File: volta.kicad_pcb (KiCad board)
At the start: 2 copper layers, 105 x 100 mm, 12 parts, among them J1 , J2 , T1 5:1 - 5A

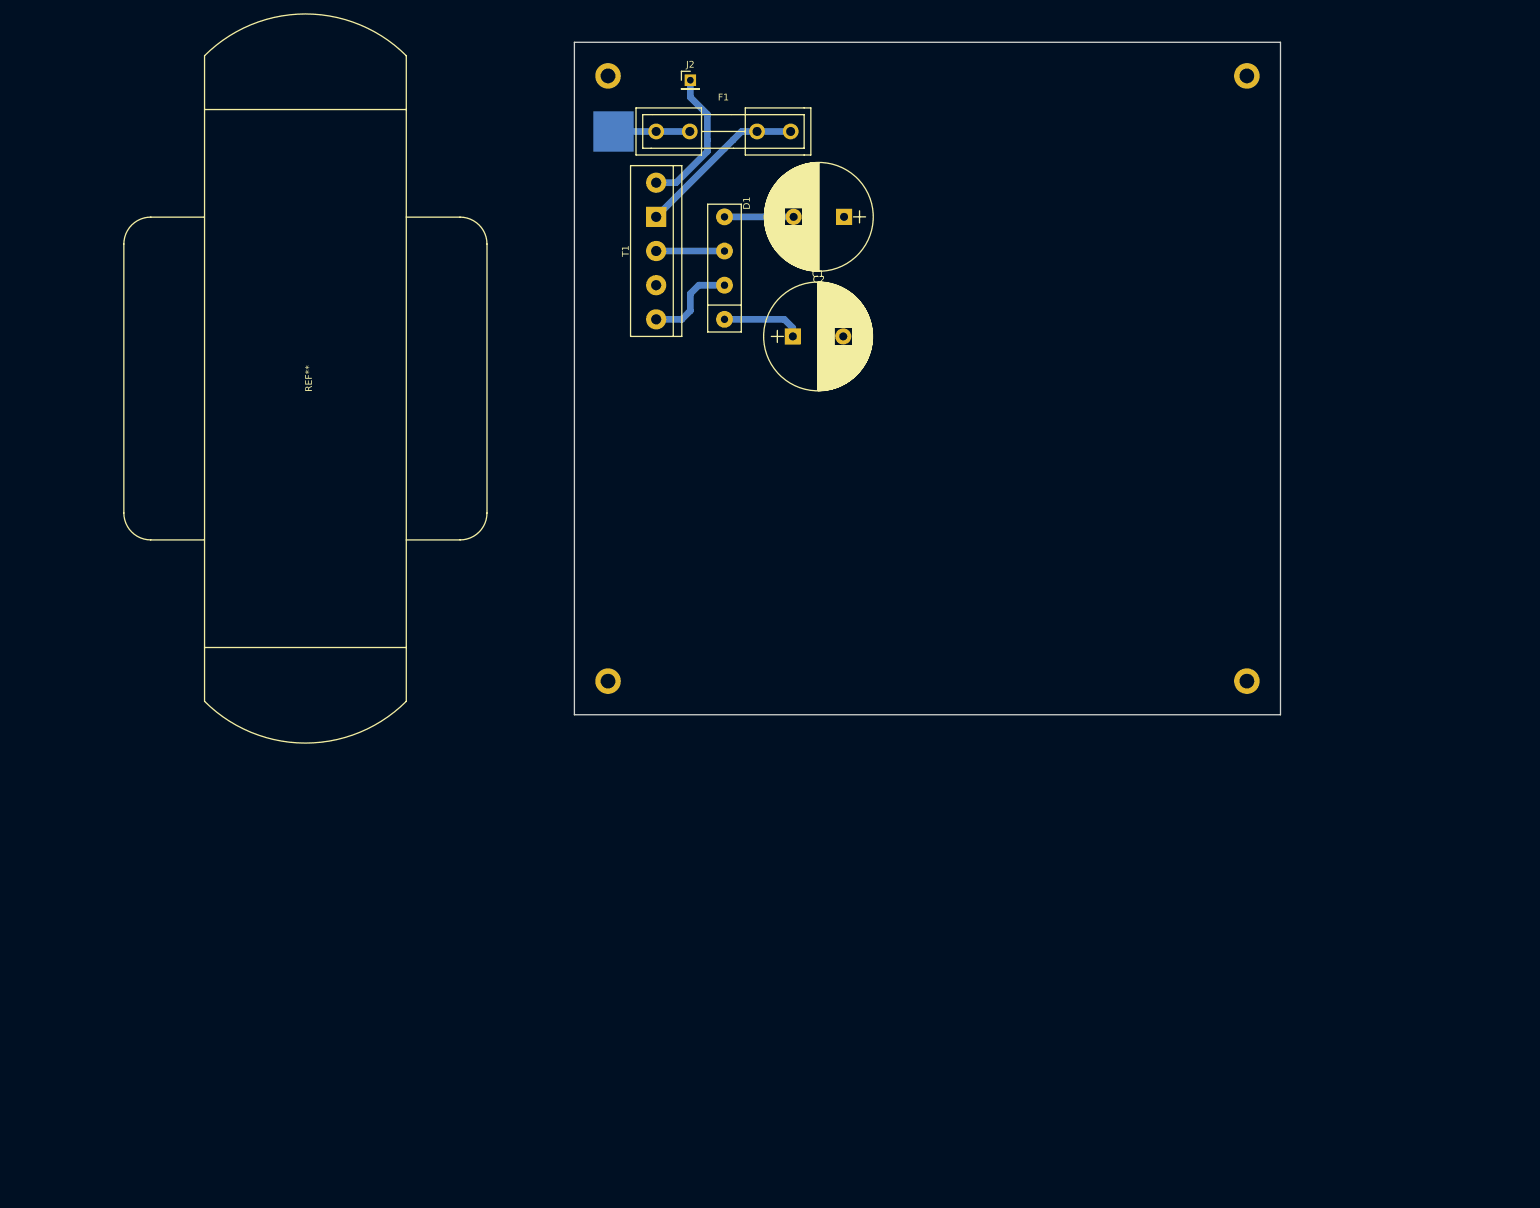
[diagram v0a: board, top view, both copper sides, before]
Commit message: Trabajo
 Cambios para hacer commit:
	modificado:    volta-cache.lib
	modificado:    volta.kicad_pcb
	modificado:    volta.pro
	modificado:    volta.sch
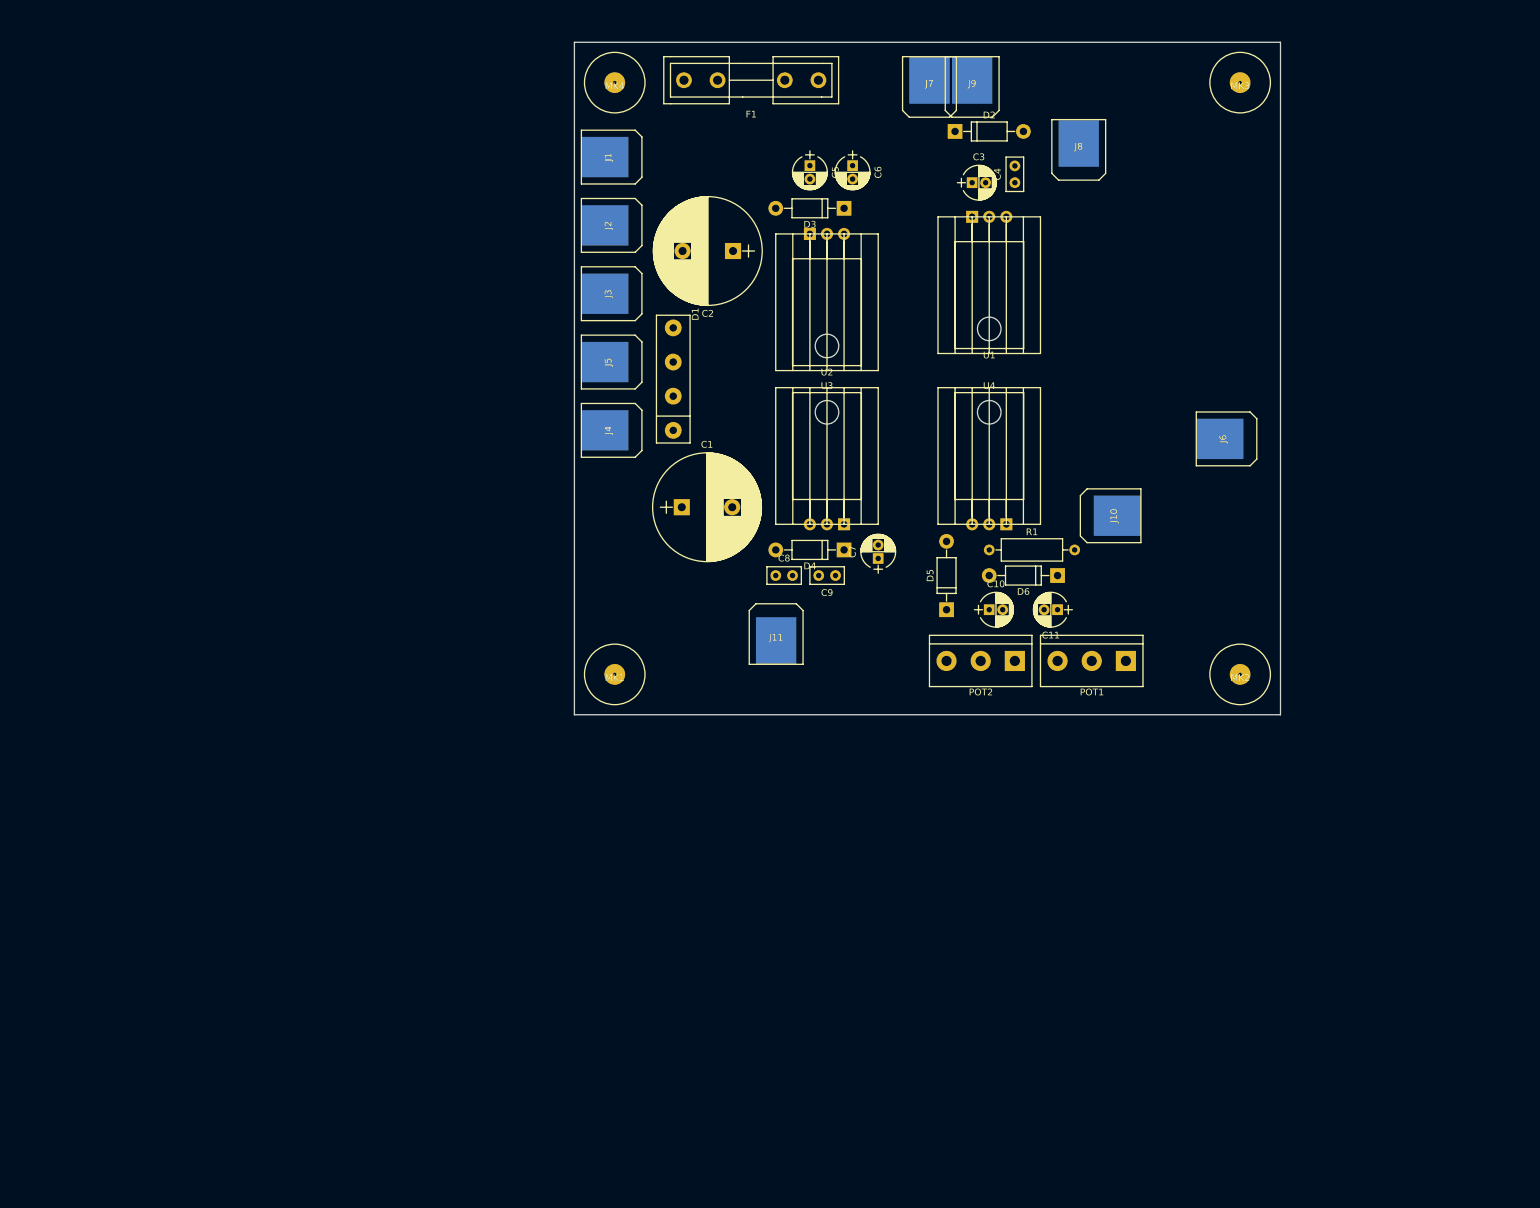
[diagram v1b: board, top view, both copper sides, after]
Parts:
- removed REF**: EXI_Transformador_1_Derivacion_80x30mm, EXI_Transformadores:EXI_Transformador_1_Derivacion_80x30mm
- removed REF** (x4): MountingHole_2.2mm_M2_DIN965_Pad, Mounting_Holes:MountingHole_2.2mm_M2_DIN965_Pad
- removed T1: 5:1 - 5A, TerminalBlock:TerminalBlock_bornier-5_P5.08mm
- added C10: 1uF, Capacitors_THT:CP_Radial_D5.0mm_P2.00mm, F.Cu at (186.7, 119.4)
- added C11: 10uF, Capacitors_THT:CP_Radial_D5.0mm_P2.00mm, F.Cu at (196.8, 119.4)
- added C3: 0.33uF, Capacitors_THT:CP_Radial_D5.0mm_P2.00mm, F.Cu at (184.2, 55.9)
- added C4: 0.1uF, Capacitors_THT:C_Disc_D5.0mm_W2.5mm_P2.50mm, F.Cu at (190.5, 55.9)
- added C5: 22uF / 25V, Capacitors_THT:CP_Radial_D5.0mm_P2.00mm, F.Cu at (160.0, 53.3)
- added C6: 1uF, Capacitors_THT:CP_Radial_D5.0mm_P2.00mm, F.Cu at (166.4, 53.3)
- added C7: 0.33uF, Capacitors_THT:CP_Radial_D5.0mm_P2.00mm, F.Cu at (170.2, 111.8)
- added C8: 0.1uF, Capacitors_THT:C_Disc_D5.0mm_W2.5mm_P2.50mm, F.Cu at (154.9, 114.3)
- added C9: 0.1uF, Capacitors_THT:C_Disc_D5.0mm_W2.5mm_P2.50mm, F.Cu at (163.8, 114.3)
- added D2: 1N4007, Diodes_THT:D_DO-41_SOD81_P10.16mm_Horizontal, F.Cu at (181.6, 48.3)
- added D3: 1N4007, Diodes_THT:D_DO-41_SOD81_P10.16mm_Horizontal, F.Cu at (165.1, 59.7)
- added D4: 1N4007, Diodes_THT:D_DO-41_SOD81_P10.16mm_Horizontal, F.Cu at (165.1, 110.5)
- added D5: 1N4007, Diodes_THT:D_DO-41_SOD81_P10.16mm_Horizontal, F.Cu at (180.3, 119.4)
- added D6: 1N4007, Diodes_THT:D_DO-41_SOD81_P10.16mm_Horizontal, F.Cu at (196.8, 114.3)
- added J10: +Vv, EXI_Conectores:EXI_Pad_6x7mm_x1, F.Cu at (205.7, 105.4)
- added J11: +5V, EXI_Conectores:EXI_Pad_6x7mm_x1, F.Cu at (155.0, 124.0)
- added J3: Deriv, EXI_Conectores:EXI_Pad_6x7mm_x1, F.Cu at (129.5, 72.4)
- added J4: Trans-V24, EXI_Conectores:EXI_Pad_6x7mm_x1, F.Cu at (129.5, 92.7)
- added J5: Trans-N24, EXI_Conectores:EXI_Pad_6x7mm_x1, F.Cu at (129.5, 82.5)
- added J6: GND, EXI_Conectores:EXI_Pad_6x7mm_x1, F.Cu at (221.0, 94.0)
- added J7: V-, EXI_Conectores:EXI_Pad_6x7mm_x1, F.Cu at (177.8, 40.6)
- added J8: +12, EXI_Conectores:EXI_Pad_6x7mm_x1, F.Cu at (200.0, 50.0)
- added J9: -12, EXI_Conectores:EXI_Pad_6x7mm_x1, F.Cu at (184.2, 40.6)
- added MK1: Mounting_Hole, EXI_Montaje:Tuerca_9mm, F.Cu at (131.0, 129.0)
- added MK2: Mounting_Hole, EXI_Montaje:Tuerca_9mm, F.Cu at (224.0, 129.0)
- added MK3: Mounting_Hole, EXI_Montaje:Tuerca_9mm, F.Cu at (224.0, 41.0)
- added MK4: Mounting_Hole, EXI_Montaje:Tuerca_9mm, F.Cu at (131.0, 41.0)
- added POT1: 5k, TerminalBlock:TerminalBlock_bornier-3_P5.08mm, F.Cu at (207.0, 127.0)
- added POT2: 1k, TerminalBlock:TerminalBlock_bornier-3_P5.08mm, F.Cu at (190.5, 127.0)
- added R1: 120, Resistors_THT:R_Axial_DIN0309_L9.0mm_D3.2mm_P12.70mm_Horizontal, F.Cu at (186.7, 110.5)
- added U1: L7812, EXI_Transistores:TO-220-3_Horizontal_Heatsink_10x15x21mm, F.Cu at (186.7, 61.0)
- added U2: L7912, EXI_Transistores:TO-220-3_Horizontal_Heatsink_10x15x21mm, F.Cu at (162.6, 63.5)
- added U3: L7805, EXI_Transistores:TO-220-3_Horizontal_Heatsink_10x15x21mm, F.Cu at (162.6, 106.7)
- added U4: LM338T, EXI_Transistores:TO-220-3_Horizontal_Heatsink_10x15x21mm, F.Cu at (186.7, 106.7)
- J1: value (none) -> AC-vivo; footprint EXI_Conectores:EXI_Pad_6x6mm -> EXI_Conectores:EXI_Pad_6x7mm_x1; moved to F.Cu
- J2: value (none) -> Trans-Vivo; footprint Pin_Headers:Pin_Header_Straight_1x01_Pitch2.54mm -> EXI_Conectores:EXI_Pad_6x7mm_x1
- moved C1 30.3 mm to (141.0, 104.1)
- moved F1 25.3 mm to (161.3, 40.6), turned to 180 degrees
- moved J2 25.0 mm to (129.5, 62.2), turned to 90 degrees
- moved D1 18.2 mm to (139.7, 85.1)
- moved C2 17.3 mm to (148.6, 66.0)
- moved J1 4.02 mm to (129.5, 52.1)
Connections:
- net Net-(C1-Pad1) renamed /V+
- net Net-(C2-Pad2) renamed /V-
- J2 pad 1: Net-(J2-Pad1) -> Net-(F1-Pad2)
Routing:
- net Net-(F1-Pad2): track 25.3 -> 0.00 mm
- net Net-(J2-Pad1): track 21.2 -> 0.00 mm
- net Net-(D1-Pad2): track 13.8 -> 0.00 mm
- net /V+: track 12.0 -> 0.00 mm
- net Net-(F1-Pad1): track 11.3 -> 0.00 mm
- net /V-: track 10.3 -> 0.00 mm
- net Net-(D1-Pad3): track 10.2 -> 0.00 mm

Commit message: Cambios menores
 Cambios para hacer commit:
	agregado el modelo 3D del pin hecho en Wings3D al pcb
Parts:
- J1: footprint EXI_Conectores:EXI_Pad_6x7mm_x1 -> EXI_Conectores:terminal_faston_0.25
- moved J1 2.54 mm to (132.1, 52.1), turned to 180 degrees
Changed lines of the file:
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@@
-  )
-  (module EXI_Conectores:EXI_Pad_6x7mm_x1 (layer F.Cu)
-    (at 129.54 52.07 90)
-    (fp_text reference J1 (at 0 0.5 90) (layer F.SilkS)
-      (effects (font (size 1 1) (thickness 0.15)))
-    )
-    (fp_text value AC-vivo (at 0 -6 90) (layer F.Fab)
-      (effects (font (size 1 1) (thickness 0.15)))
-    )
-    (fp_line (start -4.5 -4) (end -4.5 6) (layer F.CrtYd) (width 0.15))
-    (fp_line (start -4.5 6) (end 4.5 6) (layer F.CrtYd) (width 0.15))
-    (fp_line (start 4.5 6) (end 4.5 -4) (layer F.CrtYd) (width 0.15))
-    (fp_line (start 4.5 -4) (end -4.5 -4) (layer F.CrtYd) (width 0.15))
-    (fp_line (start -4 -3.5) (end -4 4.5) (layer F.SilkS) (width 0.15))
-    (fp_line (start -4 4.5) (end -3 5.5) (layer F.SilkS) (width 0.15))
-    (fp_line (start -3 5.5) (end 3 5.5) (layer F.SilkS) (width 0.15))
-    (fp_line (start 3 5.5) (end 4 4.5) (layer F.SilkS) (width 0.15))
-    (fp_line (start 4 4.5) (end 4 -3.5) (layer F.SilkS) (width 0.15))
-    (fp_line (start 4 -3.5) (end -4 -3.5) (layer F.SilkS) (width 0.15))
-    (pad 1 smd rect (at 0 0 90) (size 6 7) (layers B.Cu)
-      (net 4 "Net-(F1-Pad1)"))
   )
   (module EXI_Conectores:EXI_Pad_6x7mm_x1 (layer F.Cu)
@@
     (pad 1 thru_hole circle (at 0 0) (size 3.1 3.1) (drill 0.5) (layers *.Mask B.Cu))
   )
+  (module EXI_Conectores:terminal_faston_0.25 (layer F.Cu)
+    (at 132.08 52.07 180)
+    (fp_text reference J1 (at 0 2.54 180) (layer F.SilkS)
+      (effects (font (size 1 1) (thickness 0.15)))
+    )
+    (fp_text value AC-vivo (at 0 -2.54 180) (layer F.Fab)
+      (effects (font (size 1 1) (thickness 0.15)))
+    )
+    (fp_line (start -6.1 -1.8) (end 6.1 -1.8) (layer F.CrtYd) (width 0.1))
+    (fp_line (start 6.1 -1.8) (end 6.1 1.8) (layer F.CrtYd) (width 0.1))
+    (fp_line (start 6.1 1.8) (end -6.1 1.8) (layer F.CrtYd) (width 0.1))
+    (fp_line (start -6.1 1.8) (end -6.1 -1.8) (layer F.CrtYd) (width 0.1))
+    (fp_line (start 5.9 -0.4) (end 5.9 0) (layer F.SilkS) (width 0.1))
+    (fp_line (start -5.9 -0.4) (end -5.9 0) (layer F.SilkS) (width 0.1))
+    (fp_line (start 4.3 1.6) (end -4.3 1.6) (layer F.SilkS) (width 0.1))
+    (fp_line (start -4.7 -1.6) (end 4.7 -1.6) (layer F.SilkS) (width 0.1))
+    (fp_arc (start 4.7 -0.4) (end 4.7 -1.6) (angle 90) (layer F.SilkS) (width 0.1))
+    (fp_arc (start 4.3 0) (end 5.9 0) (angle 90) (layer F.SilkS) (width 0.1))
+    (fp_arc (start -4.7 -0.4) (end -5.9 -0.4) (angle 90) (layer F.SilkS) (width 0.1))
+    (fp_arc (start -4.3 0) (end -4.3 1.6) (angle 90) (layer F.SilkS) (width 0.1))
+    (fp_circle (center 0 0) (end 1.6 0) (layer F.SilkS) (width 0.1))
+    (pad 1 thru_hole circle (at 0 0 180) (size 2 2) (drill 0.8) (layers *.Cu *.Mask)
+      (net 4 "Net-(F1-Pad1)"))
+    (model /usr/share/kicad/EXILab/EXI_3D/exi_terminales.3dshapes/pinn.wrl
+      (at (xyz 0 0 0))
+      (scale (xyz 1 1 1))
+      (rotate (xyz 0 0 90))
+    )
+  )
   (gr_line (start 117 115) (end 117 113) (angle 90) (layer Eco2.User) (width 0.2))

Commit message: Actualización
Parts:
- removed POT1: 5k, TerminalBlock:TerminalBlock_bornier-3_P5.08mm
- removed POT2: 1k, TerminalBlock:TerminalBlock_bornier-3_P5.08mm
- added G***: UdeG11x15mm, EXI_Simbolgia:UdeG11x15mm, F.Cu at (186.4, 126.5)
- added J12: +Vv, EXI_Conectores:terminal_faston_0.25, F.Cu at (194.3, 98.4)
- added J13: +5V, EXI_Conectores:terminal_faston_0.25, F.Cu at (194.3, 89.5)
- added LED1: Activo, Pin_Headers:Pin_Header_Straight_1x02_Pitch2.54mm, F.Cu at (147.3, 123.2)
- added R2: 470, Resistors_THT:R_Axial_DIN0309_L9.0mm_D3.2mm_P12.70mm_Horizontal, F.Cu at (163.8, 123.2)
- added V1: EXI_Ventilador, Pin_Headers:Pin_Header_Straight_1x02_Pitch2.54mm, F.Cu at (147.3, 119.4)
- C10: footprint Capacitors_THT:CP_Radial_D5.0mm_P2.00mm -> Capacitors_THT:CP_Radial_D5.0mm_P2.50mm
- C11, C3, C5, C6, C7: footprint Capacitors_THT:CP_Radial_D5.0mm_P2.00mm -> EXI_Condensadores:CP_Radial_D5.0mm_P2.00mm
- C4, C8, C9: footprint Capacitors_THT:C_Disc_D5.0mm_W2.5mm_P2.50mm -> EXI_Condensadores:C_Disc_D5.0mm_W2.5mm_P2.50mm
- D5, D6: footprint Diodes_THT:D_DO-41_SOD81_P10.16mm_Horizontal -> Diodes_THT:D_DO-41_SOD81_P5.08mm_Vertical_KathodeUp
- J10: value +Vv -> +12; footprint EXI_Conectores:EXI_Pad_6x7mm_x1 -> EXI_Conectores:terminal_faston_0.25
- J11: value +5V -> -12; footprint EXI_Conectores:EXI_Pad_6x7mm_x1 -> EXI_Conectores:terminal_faston_0.25
- J2: footprint EXI_Conectores:EXI_Pad_6x7mm_x1 -> EXI_Conectores:terminal_faston_0.25
- J3: value Deriv -> Trans-V24; footprint EXI_Conectores:EXI_Pad_6x7mm_x1 -> EXI_Conectores:terminal_faston_0.25
- J4: value Trans-V24 -> Trans-N24; footprint EXI_Conectores:EXI_Pad_6x7mm_x1 -> EXI_Conectores:terminal_faston_0.25
- J5: value Trans-N24 -> Deriv; footprint EXI_Conectores:EXI_Pad_6x7mm_x1 -> EXI_Conectores:terminal_faston_0.25
- J6: value GND -> Pot_adj; footprint EXI_Conectores:EXI_Pad_6x7mm_x1 -> EXI_Conectores:terminal_faston_0.25
- J7: value V- -> Pot_gnd; footprint EXI_Conectores:EXI_Pad_6x7mm_x1 -> EXI_Conectores:terminal_faston_0.25
- J8: value +12 -> GND; footprint EXI_Conectores:EXI_Pad_6x7mm_x1 -> EXI_Conectores:terminal_faston_0.25
- J9: value -12 -> V-; footprint EXI_Conectores:EXI_Pad_6x7mm_x1 -> EXI_Conectores:terminal_faston_0.25
- R1: footprint Resistors_THT:R_Axial_DIN0309_L9.0mm_D3.2mm_P12.70mm_Horizontal -> Resistors_THT:R_Axial_DIN0309_L9.0mm_D3.2mm_P5.08mm_Vertical
- moved J11 72.7 mm to (194.3, 62.9), turned to 0 degrees
- moved J7 68.7 mm to (194.3, 107.3)
- moved J10 52.7 mm to (194.3, 54.0), turned to 0 degrees
- moved J1 51.8 mm to (182.9, 41.9), turned to 90 degrees
- moved J9 41.3 mm to (194.3, 80.6)
- moved J6 34.7 mm to (194.3, 116.2), turned to 0 degrees
- moved MK2 26.0 mm to (198.0, 129.0)
- moved MK3 26.0 mm to (198.0, 41.0)
- moved J2 24.0 mm to (142.2, 41.9)
- moved J8 22.5 mm to (194.3, 71.8)
- moved J3 22.2 mm to (134.6, 94.0), turned to 0 degrees
- moved D6 20.9 mm to (177.8, 122.9)
- moved J4 17.3 mm to (134.6, 76.2), turned to 0 degrees
- moved R1 16.3 mm to (172.7, 118.9)
- moved C11 15.9 mm to (181.6, 114.9), turned to 90 degrees
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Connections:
- net Net-(F1-Pad1) renamed /sw
- net Net-(F1-Pad2) renamed /trans
- C11 pad 1: Net-(C11-Pad1) -> /adj
- D1 pad 2: Net-(D1-Pad2) -> /v24
- D1 pad 3: Net-(D1-Pad3) -> /n24
- D6 pad 1: Net-(C11-Pad1) -> /adj
- J10 pad 1: /+Vv -> /+12
- J11 pad 1: /+5V -> /-12
- J3 pad 1: GND -> /v24
- J4 pad 1: Net-(D1-Pad2) -> /n24
- J5 pad 1: Net-(D1-Pad3) -> GND
- J6 pad 1: GND -> /adj
- J7 pad 1: /V- -> /comun
- J8 pad 1: /+12 -> GND
- J9 pad 1: /-12 -> /V-
- R1 pad 2: Net-(C11-Pad1) -> /adj
- U4 pad 1: Net-(C11-Pad1) -> /adj
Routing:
- net /V+: track 0.00 -> 209.6 mm
- net /comun: track 0.00 -> 110.9 mm
- net /V-: track 0.00 -> 109.1 mm
- net /+5V: track 0.00 -> 86.7 mm
- net /-12: track 0.00 -> 63.8 mm
- net /adj: track 0.00 -> 54.3 mm
- net /+Vv: track 0.00 -> 47.5 mm
- net /+12: track 0.00 -> 29.4 mm
- net /sw: track 0.00 -> 16.4 mm
- net /v24: track 0.00 -> 15.0 mm
- net /n24: track 0.00 -> 15.0 mm
- net /trans: track 0.00 -> 14.2 mm
- net Net-(LED1-Pad1): track 0.00 -> 3.81 mm
- added copper zone on B.Cu, net GND
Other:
- board size 105 x 100 mm -> 79 x 100 mm
- net class 120ac removed
- net class 4A added: clearance 0.5, trace_width 2.1, via_dia 3, via_drill 0.8
- net class Default: clearance 0.5 -> 0.2; via_dia 1.2 -> 2
- rule trace_clearance: 0.5 -> 0.2
- board text added: "+"
- board text added: "+12"
- board text added: "+5"
- board text added: "-"
- board text added: "-12"
- board text added: "Centro Universitario de la Costa Sur"
- board text added: "Depto. de Ingenierías"
- board text added: "Deriv"
- board text added: "Linea"
- board text added: "POT"
- board text added: "SALIDAS"
- board text added: "TFV-180417-LACRA"
- board text added: "Tr-1"
- board text added: "Tr-2"
- board text added: "Transf"
- board text added: "V-"
- board text added: "Var"
- board text added: "adj"
- board text added: "cmn"
- board text added: "gnd"
